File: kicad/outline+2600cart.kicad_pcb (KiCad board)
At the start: 2 copper layers, 41.3 x 46.9 mm, 4 parts, among them U1 2600Cartridge, U2 74LS04, U3 2732

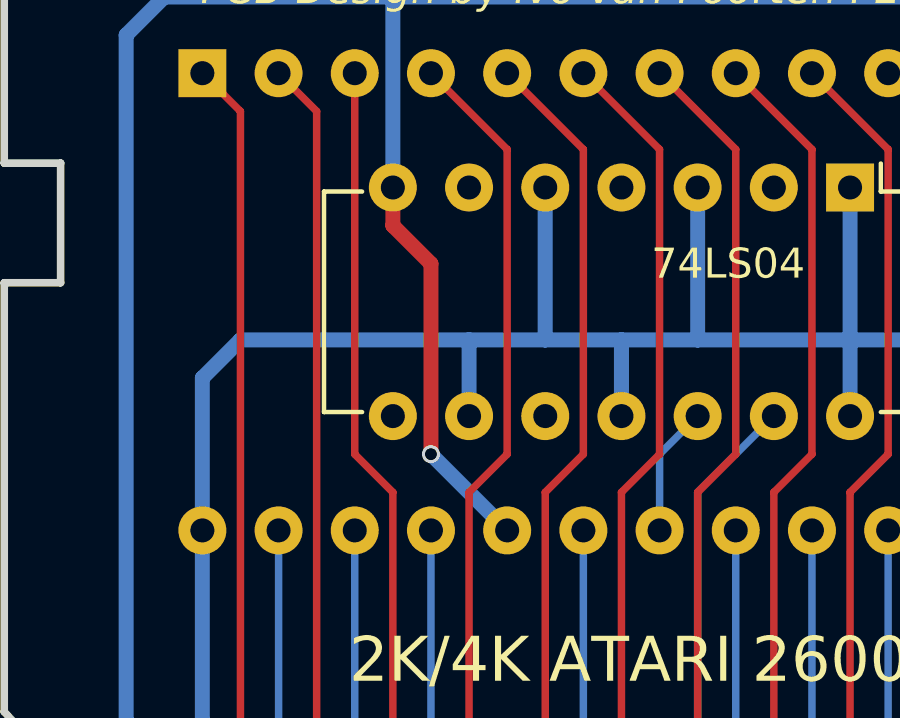
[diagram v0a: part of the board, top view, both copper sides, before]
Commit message: remove useless track and via in combined project. it has now zero vias :)
also

don't track fp-info-cache anymore
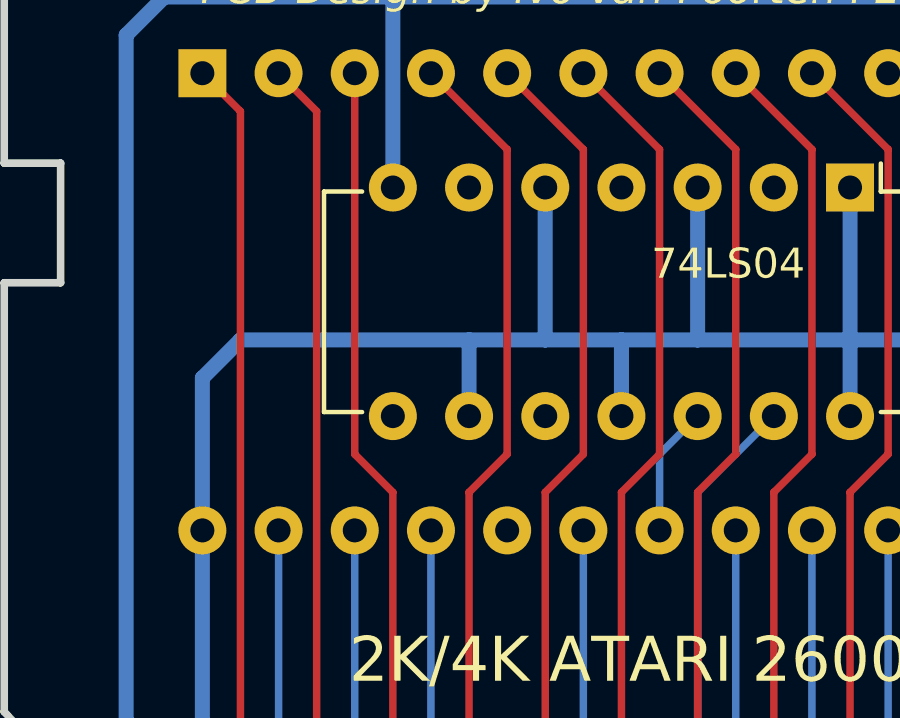
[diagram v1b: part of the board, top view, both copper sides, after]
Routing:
- net GND: track 133.6 -> 120.5 mm, vias 1 -> 0
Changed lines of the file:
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@@
     (thickness 1.6)
     (drawings 23)
-    (tracks 117)
+    (tracks 112)
     (zones 0)
     (modules 4)
@@
       (effects (font (size 1 1) (thickness 0.15)) (justify mirror))
     )
+    (fp_line (start -1.05 2.45) (end -1.05 -30.4) (layer B.CrtYd) (width 0.05))
+    (fp_line (start 16.3 2.45) (end 16.3 -30.4) (layer B.CrtYd) (width 0.05))
+    (fp_line (start -1.05 2.45) (end 16.3 2.45) (layer B.CrtYd) (width 0.05))
+    (fp_line (start -1.05 -30.4) (end 16.3 -30.4) (layer B.CrtYd) (width 0.05))
+    (fp_line (start 0.135 2.295) (end 0.135 1.025) (layer B.SilkS) (width 0.15))
+    (fp_line (start 15.105 2.295) (end 15.105 1.025) (layer B.SilkS) (width 0.15))
+    (fp_line (start 15.105 -30.235) (end 15.105 -28.965) (layer B.SilkS) (width 0.15))
+    (fp_line (start 0.135 -30.235) (end 0.135 -28.965) (layer B.SilkS) (width 0.15))
+    (fp_line (start 0.135 2.295) (end 15.105 2.295) (layer B.SilkS) (width 0.15))
+    (fp_line (start 0.135 -30.235) (end 15.105 -30.235) (layer B.SilkS) (width 0.15))
     (fp_line (start 0.135 1.025) (end -0.8 1.025) (layer B.SilkS) (width 0.15))
-    (fp_line (start 0.135 -30.235) (end 15.105 -30.235) (layer B.SilkS) (width 0.15))
-    (fp_line (start 0.135 2.295) (end 15.105 2.295) (layer B.SilkS) (width 0.15))
-    (fp_line (start 0.135 -30.235) (end 0.135 -28.965) (layer B.SilkS) (width 0.15))
-    (fp_line (start 15.105 -30.235) (end 15.105 -28.965) (layer B.SilkS) (width 0.15))
-    (fp_line (start 15.105 2.295) (end 15.105 1.025) (layer B.SilkS) (width 0.15))
-    (fp_line (start 0.135 2.295) (end 0.135 1.025) (layer B.SilkS) (width 0.15))
-    (fp_line (start -1.05 -30.4) (end 16.3 -30.4) (layer B.CrtYd) (width 0.05))
-    (fp_line (start -1.05 2.45) (end 16.3 2.45) (layer B.CrtYd) (width 0.05))
-    (fp_line (start 16.3 2.45) (end 16.3 -30.4) (layer B.CrtYd) (width 0.05))
-    (fp_line (start -1.05 2.45) (end -1.05 -30.4) (layer B.CrtYd) (width 0.05))
     (pad 1 thru_hole rect (at 0 0 270) (size 1.6 1.6) (drill 0.8) (layers *.Cu *.Mask B.SilkS)
       (net 5 A7))
@@
       (effects (font (size 1 1) (thickness 0.15)))
     )
+    (fp_line (start -0.9 -1.5) (end 3.4 -1.5) (layer F.CrtYd) (width 0.05))
+    (fp_line (start 3.4 -1.5) (end 3.4 1.5) (layer F.CrtYd) (width 0.05))
+    (fp_line (start 3.4 1.5) (end -0.9 1.5) (layer F.CrtYd) (width 0.05))
+    (fp_line (start -0.9 1.5) (end -0.9 -1.5) (layer F.CrtYd) (width 0.05))
+    (fp_line (start -0.25 -1.25) (end 2.75 -1.25) (layer F.SilkS) (width 0.15))
     (fp_line (start 2.75 1.25) (end -0.25 1.25) (layer F.SilkS) (width 0.15))
-    (fp_line (start -0.25 -1.25) (end 2.75 -1.25) (layer F.SilkS) (width 0.15))
-    (fp_line (start -0.9 1.5) (end -0.9 -1.5) (layer F.CrtYd) (width 0.05))
-    (fp_line (start 3.4 1.5) (end -0.9 1.5) (layer F.CrtYd) (width 0.05))
-    (fp_line (start 3.4 -1.5) (end 3.4 1.5) (layer F.CrtYd) (width 0.05))
-    (fp_line (start -0.9 -1.5) (end 3.4 -1.5) (layer F.CrtYd) (width 0.05))
     (pad 1 thru_hole oval (at 0 0 90) (size 1.3 1.3) (drill 0.8) (layers *.Cu *.Mask F.SilkS)
       (net 1 VCC))
@@
       (effects (font (size 1 1) (thickness 0.15)))
     )
+    (fp_line (start -1.05 -2.45) (end -1.05 17.7) (layer F.CrtYd) (width 0.05))
+    (fp_line (start 8.65 -2.45) (end 8.65 17.7) (layer F.CrtYd) (width 0.05))
+    (fp_line (start -1.05 -2.45) (end 8.65 -2.45) (layer F.CrtYd) (width 0.05))
+    (fp_line (start -1.05 17.7) (end 8.65 17.7) (layer F.CrtYd) (width 0.05))
+    (fp_line (start 0.135 -2.295) (end 0.135 -1.025) (layer F.SilkS) (width 0.15))
+    (fp_line (start 7.485 -2.295) (end 7.485 -1.025) (layer F.SilkS) (width 0.15))
+    (fp_line (start 7.485 17.535) (end 7.485 16.265) (layer F.SilkS) (width 0.15))
+    (fp_line (start 0.135 17.535) (end 0.135 16.265) (layer F.SilkS) (width 0.15))
+    (fp_line (start 0.135 -2.295) (end 7.485 -2.295) (layer F.SilkS) (width 0.15))
+    (fp_line (start 0.135 17.535) (end 7.485 17.535) (layer F.SilkS) (width 0.15))
     (fp_line (start 0.135 -1.025) (end -0.8 -1.025) (layer F.SilkS) (width 0.15))
-    (fp_line (start 0.135 17.535) (end 7.485 17.535) (layer F.SilkS) (width 0.15))
-    (fp_line (start 0.135 -2.295) (end 7.485 -2.295) (layer F.SilkS) (width 0.15))
-    (fp_line (start 0.135 17.535) (end 0.135 16.265) (layer F.SilkS) (width 0.15))
-    (fp_line (start 7.485 17.535) (end 7.485 16.265) (layer F.SilkS) (width 0.15))
-    (fp_line (start 7.485 -2.295) (end 7.485 -1.025) (layer F.SilkS) (width 0.15))
-    (fp_line (start 0.135 -2.295) (end 0.135 -1.025) (layer F.SilkS) (width 0.15))
-    (fp_line (start -1.05 17.7) (end 8.65 17.7) (layer F.CrtYd) (width 0.05))
-    (fp_line (start -1.05 -2.45) (end 8.65 -2.45) (layer F.CrtYd) (width 0.05))
-    (fp_line (start 8.65 -2.45) (end 8.65 17.7) (layer F.CrtYd) (width 0.05))
-    (fp_line (start -1.05 -2.45) (end -1.05 17.7) (layer F.CrtYd) (width 0.05))
     (pad 1 thru_hole rect (at 0 0 270) (size 1.6 1.6) (drill 0.8) (layers *.Cu *.Mask F.SilkS)
       (net 1 VCC))
@@
   (segment (start 98.044 88.9) (end 98.044 74.93) (width 0.5) (layer B.Cu) (net 1))
   (segment (start 98.044 74.93) (end 95.504 72.39) (width 0.5) (layer B.Cu) (net 1))
-  (segment (start 101.854 54.61) (end 101.854 55.88) (width 0.5) (layer F.Cu) (net 2))
-  (segment (start 101.854 55.88) (end 103.124 57.15) (width 0.5) (layer F.Cu) (net 2))
-  (segment (start 103.124 57.15) (end 103.124 63.5) (width 0.5) (layer F.Cu) (net 2))
-  (via (at 103.124 63.5) (size 0.6) (drill 0.4) (layers F.Cu B.Cu) (net 2))
-  (segment (start 103.124 63.5) (end 105.664 66.04) (width 0.5) (layer B.Cu) (net 2))
   (segment (start 95.504 88.9) (end 95.504 74.93) (width 0.5) (layer B.Cu) (net 2))
   (segment (start 94.234 48.26) (end 101.854 48.26) (width 0.5) (layer B.Cu) (net 2))
